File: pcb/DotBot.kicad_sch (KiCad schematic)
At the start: 44 parts, among them J1 Shield Header, J10 Extra Pins, J11 Motor connector, J12 Motor connector, J6 SWD, J7 Shield Header, J8 Extra Pins, J9 Extra Pins, Q3 DMP2045U-7, Q4 DMP2045U-7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

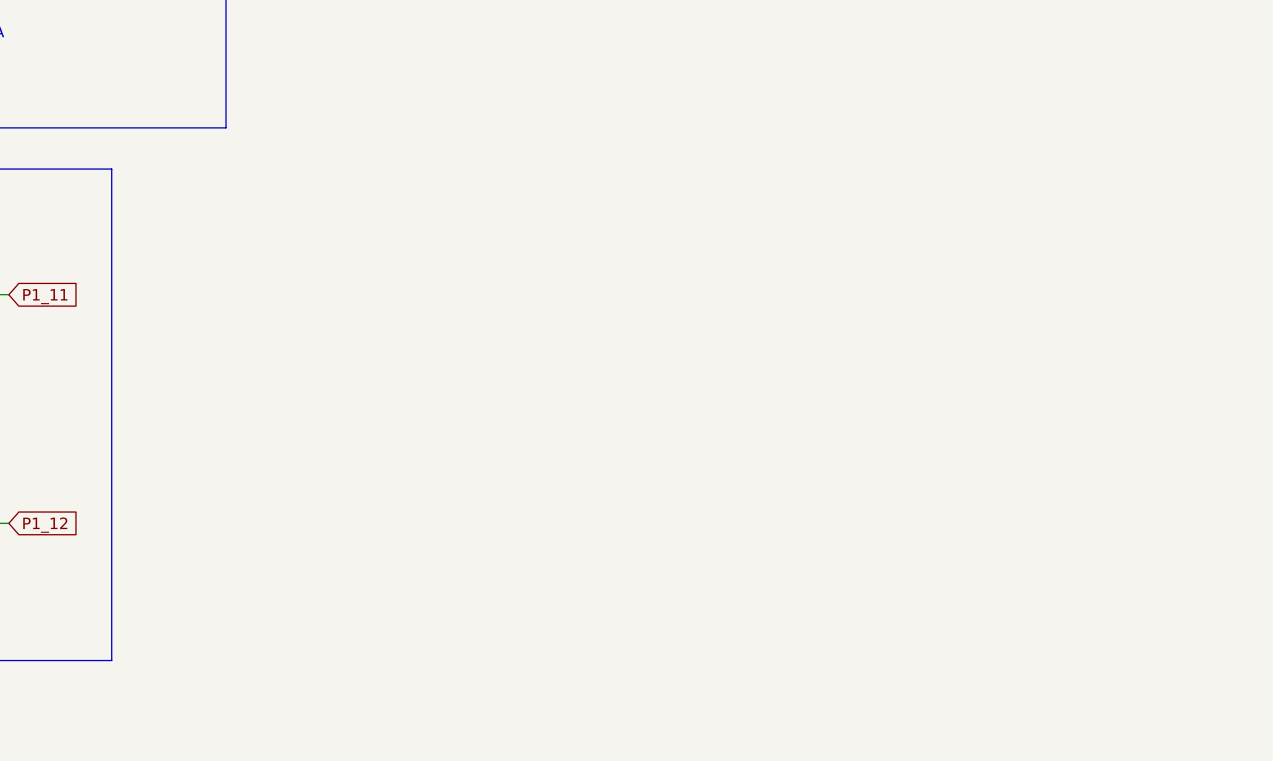
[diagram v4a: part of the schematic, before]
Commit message: #11 3v-motor: add RGB LED to the main board
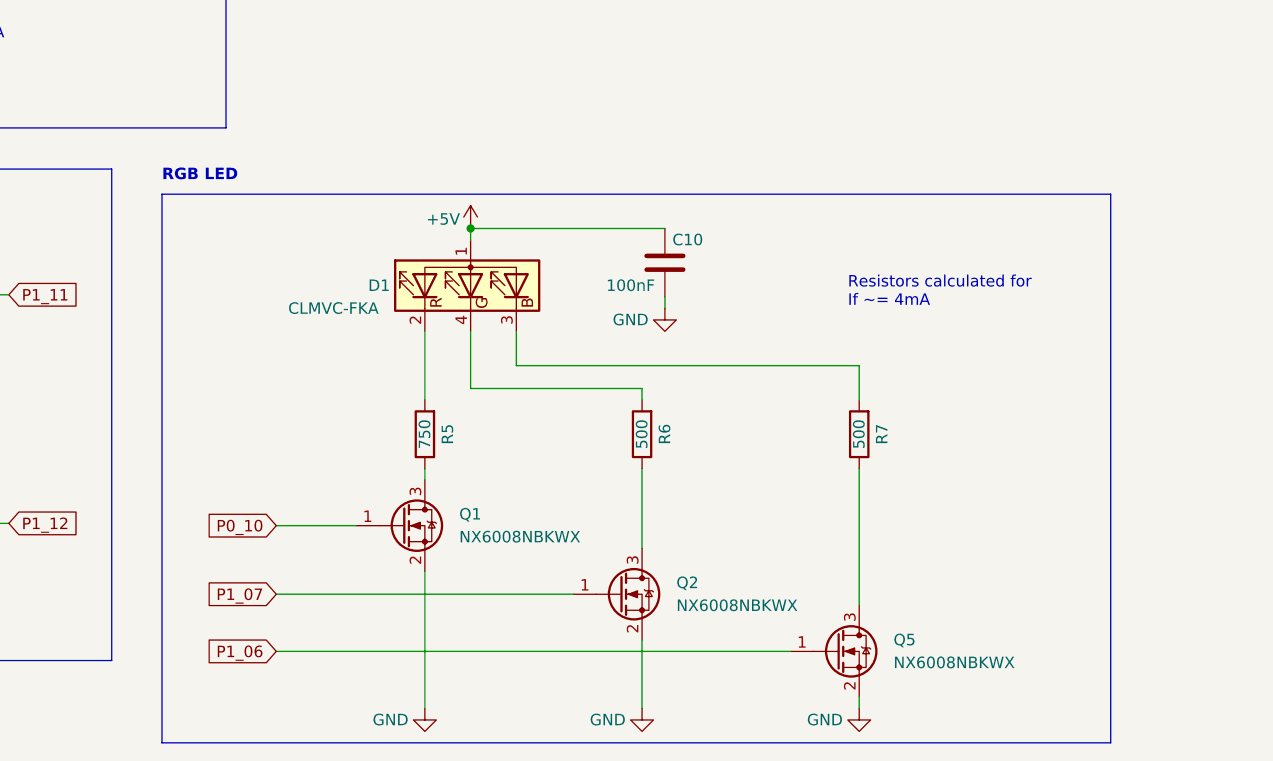
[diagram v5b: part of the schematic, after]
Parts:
- added C10: 100nF, Capacitor_SMD:C_0603_1608Metric, symbol Device:C
- added D1: CLMVC-FKA, LED_SMD:LED_Cree-PLCC4_2x2mm_CW, symbol Device:LED_ARBG
- added Q1, Q2, Q5: NX6008NBKWX, Package_TO_SOT_SMD:SOT-323_SC-70, symbol Device:Q_NMOS_GSD
- added R5: 750, Resistor_SMD:R_0603_1608Metric, symbol Device:R
- added R6, R7: 500, Resistor_SMD:R_0603_1608Metric, symbol Device:R
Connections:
- net +5V: now also C10.1, D1.1 (A)
- net GND: now also C10.2, Q1.2 (S), Q2.2 (S), Q5.2 (S)
- net P0_10: now also Q1.1 (G)
- net P1_06: now also Q5.1 (G)
- net P1_07: now also Q2.1 (G)
- new net: Q2.3 (D), R6.1
- new net: D1.4 (GK), R6.2
- new net: Q5.3 (D), R7.1
- new net: Q1.3 (D), R5.1
- new net: D1.2 (RK), R5.2
- new net: D1.3 (BK), R7.2
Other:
- note added: "RGB LED"
- note added: "Resistors calculated for If ~= 4mA"

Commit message: #11 3v-motor: Add left and right tags to the shield header schematic
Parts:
- J1: value Shield Header -> Left Shield Header
- J7: value Shield Header -> Right Shield Header
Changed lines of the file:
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@@
       (effects (font (size 1.27 1.27)))
     )
-    (property "Value" "Shield Header" (at 68.58 41.91 90)
+    (property "Value" "Right Shield Header" (at 68.58 41.91 90)
       (effects (font (size 1.27 1.27)))
     )
@@
       (effects (font (size 1.27 1.27)))
     )
-    (property "Value" "Shield Header" (at 38.1 41.91 90)
-      (effects (font (size 1.27 1.27)))
-    )
+    (property "Value" "Left Shield Header" (at 38.1 41.91 90)
+      (effects (font (size 1.27 1.27)))
+    )

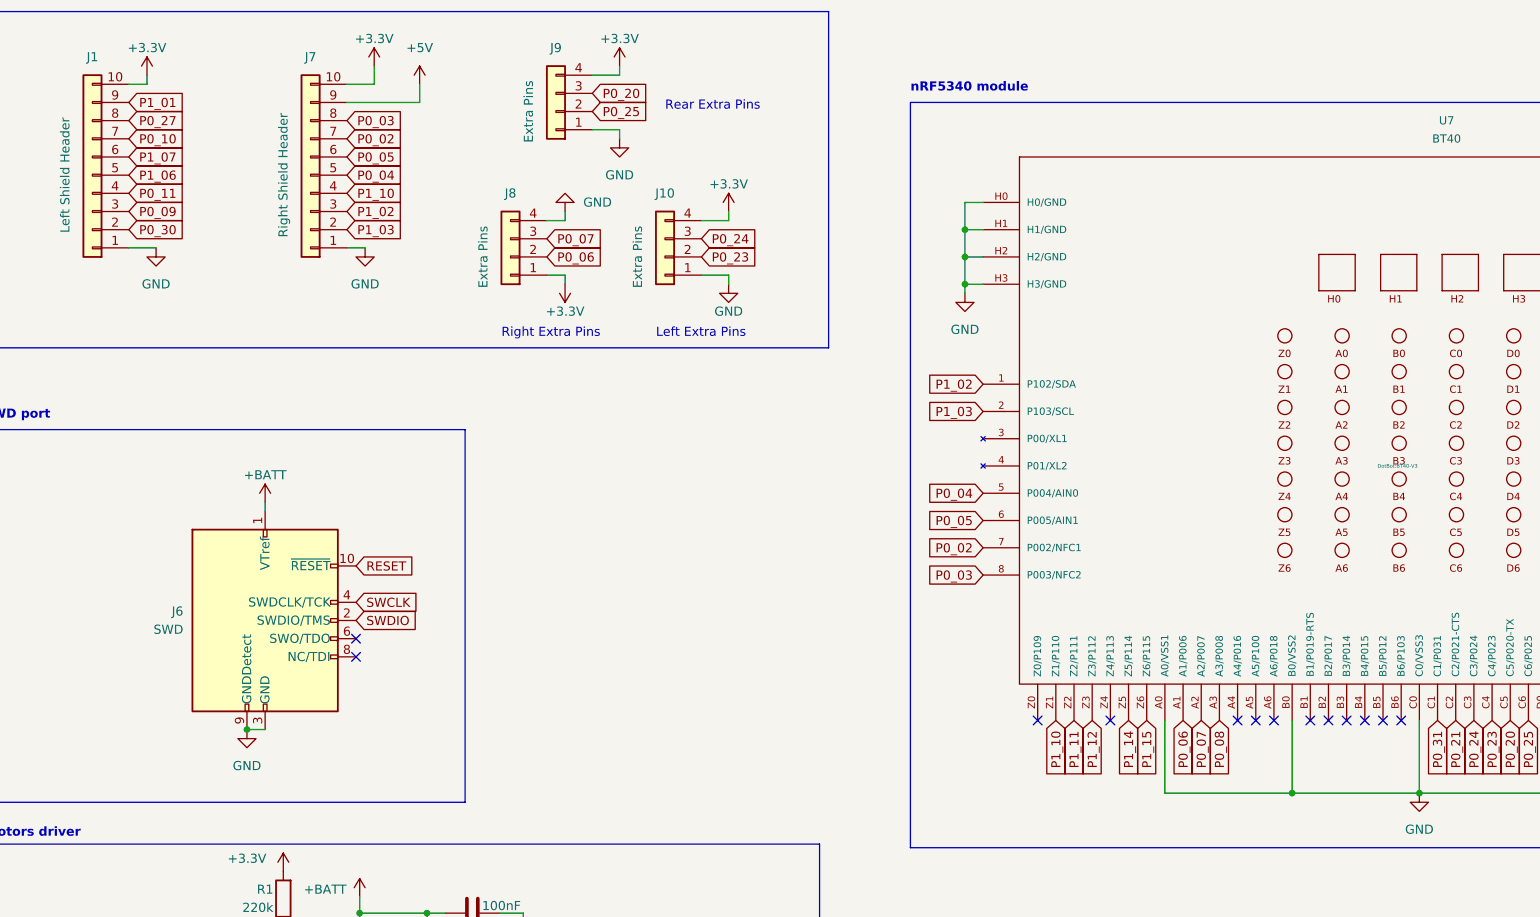
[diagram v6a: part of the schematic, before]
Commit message: #11 3v-motor: reassign the RGB shield pin to 3 unused pins
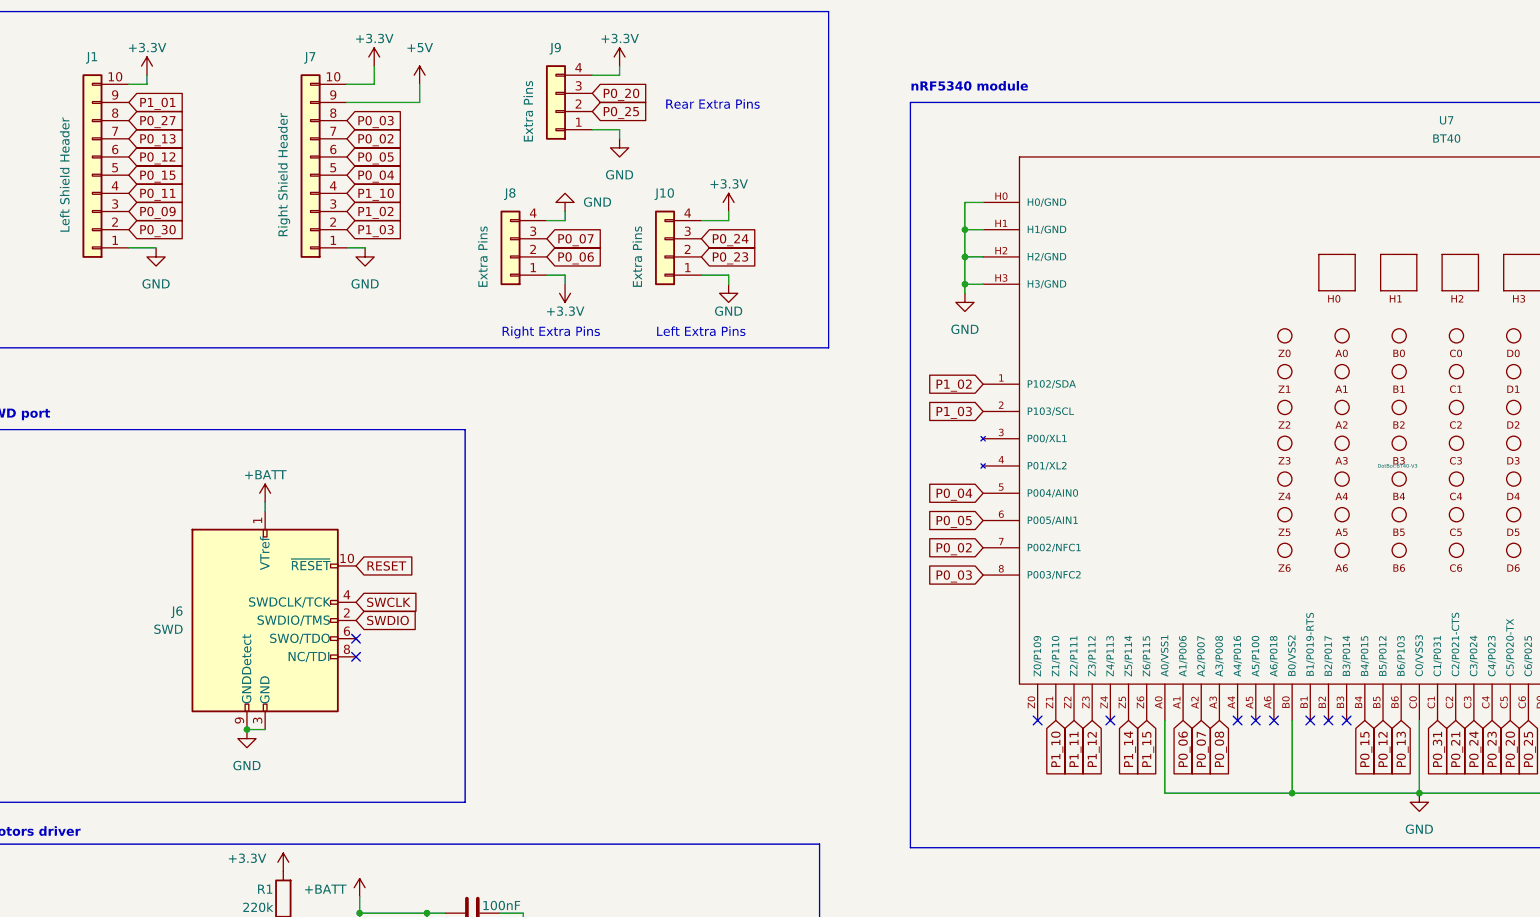
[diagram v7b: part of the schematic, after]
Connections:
- net P0_10: no longer J1.7 (Pin_7)
- net P1_06: no longer J1.5 (Pin_5)
- net P1_07: no longer J1.6 (Pin_6)
- net P0_15: now reaches U7.B4 (B4/P015)
- net P0_15: now also J1.5 (Pin_5)
- net P0_12: now reaches U7.B5 (B5/P012)
- net P0_12: now also J1.6 (Pin_6)
- net P0_13: now reaches U7.B6 (B6/P103)
- net P0_13: now also J1.7 (Pin_7)
- no-connect marks 19 -> 16
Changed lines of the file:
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@@
   (junction (at 93.98 254) (diameter 0) (color 0 0 0 0)
   )
-  (no_connect (at 224.79 118.11))
   (no_connect (at 184.15 118.11))
   (no_connect (at 212.09 118.11))
-  (no_connect (at 219.71 118.11))
   (no_connect (at 288.29 118.11))
   (no_connect (at 78.74 109.22))
@@
   (no_connect (at 99.568 162.814))
   (no_connect (at 201.93 118.11))
-  (no_connect (at 222.25 118.11))
   (no_connect (at 280.67 118.11))
   (no_connect (at 285.75 118.11))
@@
     )
   )
-  (global_label "P1_06" (shape input) (at 46.99 41.91 0) (fields_autoplaced)
-    (effects (font (size 1.27 1.27)) (justify left))
-    (property "Intersheetrefs" "${INTERSHEET_REFS}" (at 55.7619 41.91 0)
-      (effects (font (size 1.27 1.27)) (justify left) hide)
-    )
-  )
   (global_label "P0_29" (shape input) (at 104.394 180.086 0) (fields_autoplaced)
     (effects (font (size 1.27 1.27)) (justify left))
@@
     )
   )
-  (global_label "P1_07" (shape input) (at 46.99 39.37 0) (fields_autoplaced)
-    (effects (font (size 1.27 1.27)) (justify left))
-    (property "Intersheetrefs" "${INTERSHEET_REFS}" (at 55.7619 39.37 0)
-      (effects (font (size 1.27 1.27)) (justify left) hide)
-    )
-  )
   (global_label "P1_03" (shape input) (at 77.47 49.53 0) (fields_autoplaced)
     (effects (font (size 1.27 1.27)) (justify left))
@@
     )
   )
+  (global_label "P0_15" (shape input) (at 219.71 118.11 270) (fields_autoplaced)
+    (effects (font (size 1.27 1.27)) (justify right))
+    (property "Intersheetrefs" "${INTERSHEET_REFS}" (at 219.71 126.9613 90)
+      (effects (font (size 1.27 1.27)) (justify right) hide)
+    )
+  )
   (global_label "P1_11" (shape input) (at 179.07 118.11 270) (fields_autoplaced)
     (effects (font (size 1.27 1.27)) (justify right))
@@
     )
   )
+  (global_label "P0_13" (shape input) (at 46.99 36.83 0) (fields_autoplaced)
+    (effects (font (size 1.27 1.27)) (justify left))
+    (property "Intersheetrefs" "${INTERSHEET_REFS}" (at 55.8413 36.83 0)
+      (effects (font (size 1.27 1.27)) (justify left) hide)
+    )
+  )
   (global_label "P1_06" (shape input) (at 149.098 264.414 180) (fields_autoplaced)
     (effects (font (size 1.27 1.27)) (justify right))
@@
     )
   )
+  (global_label "P0_13" (shape input) (at 224.79 118.11 270) (fields_autoplaced)
+    (effects (font (size 1.27 1.27)) (justify right))
+    (property "Intersheetrefs" "${INTERSHEET_REFS}" (at 224.79 126.9613 90)
+      (effects (font (size 1.27 1.27)) (justify right) hide)
+    )
+  )
+  (global_label "P0_12" (shape input) (at 222.25 118.11 270) (fields_autoplaced)
+    (effects (font (size 1.27 1.27)) (justify right))
+    (property "Intersheetrefs" "${INTERSHEET_REFS}" (at 222.25 126.9613 90)
+      (effects (font (size 1.27 1.27)) (justify right) hide)
+    )
+  )
   (global_label "P0_02" (shape input) (at 166.37 93.98 180) (fields_autoplaced)
     (effects (font (size 1.27 1.27)) (justify right))
@@
     )
   )
+  (global_label "P0_15" (shape input) (at 46.99 41.91 0) (fields_autoplaced)
+    (effects (font (size 1.27 1.27)) (justify left))
+    (property "Intersheetrefs" "${INTERSHEET_REFS}" (at 55.8413 41.91 0)
+      (effects (font (size 1.27 1.27)) (justify left) hide)
+    )
+  )
   (global_label "P1_10" (shape input) (at 77.47 44.45 0) (fields_autoplaced)
     (effects (font (size 1.27 1.27)) (justify left))
@@
     )
   )
-  (global_label "P0_10" (shape input) (at 46.99 36.83 0) (fields_autoplaced)
-    (effects (font (size 1.27 1.27)) (justify left))
-    (property "Intersheetrefs" "${INTERSHEET_REFS}" (at 55.7619 36.83 0)
-      (effects (font (size 1.27 1.27)) (justify left) hide)
-    )
-  )
   (global_label "P0_26" (shape input) (at 247.65 118.11 270) (fields_autoplaced)
     (effects (font (size 1.27 1.27)) (justify right))
@@
       (effects (font (size 1.27 1.27)) (justify left) hide)
     )
+  )
+  (global_label "P0_12" (shape input) (at 46.99 39.37 0) (fields_autoplaced)
+    (effects (font (size 1.27 1.27)) (justify left))
+    (property "Intersheetrefs" "${INTERSHEET_REFS}" (at 55.8413 39.37 0)
+      (effects (font (size 1.27 1.27)) (justify left) hide)
+    )

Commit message: #11 3v-motor: change motor driver footprint to QFN package
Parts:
- U6: footprint Package_SO:HTSSOP-16-1EP_4.4x5mm_P0.65mm_EP3.4x5mm_Mask2.46x2.31mm_ThermalVias -> Package_DFN_QFN:WQFN-16-1EP_3x3mm_P0.5mm_EP1.6x1.6mm_ThermalVias
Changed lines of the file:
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@@
       (effects (font (size 1.27 1.27)) (justify left))
     )
-    (property "Footprint" "Package_SO:HTSSOP-16-1EP_4.4x5mm_P0.65mm_EP3.4x5mm_Mask2.46x2.31mm_ThermalVias" (at 72.898 160.782 0)
+    (property "Footprint" "Package_DFN_QFN:WQFN-16-1EP_3x3mm_P0.5mm_EP1.6x1.6mm_ThermalVias" (at 72.898 160.782 0)
       (effects (font (size 1.27 1.27)) (justify left) hide)
     )
